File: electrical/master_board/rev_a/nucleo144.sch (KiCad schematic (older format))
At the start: 1 part, among them CN95 NUCLEO-F767ZI;2xF2x35

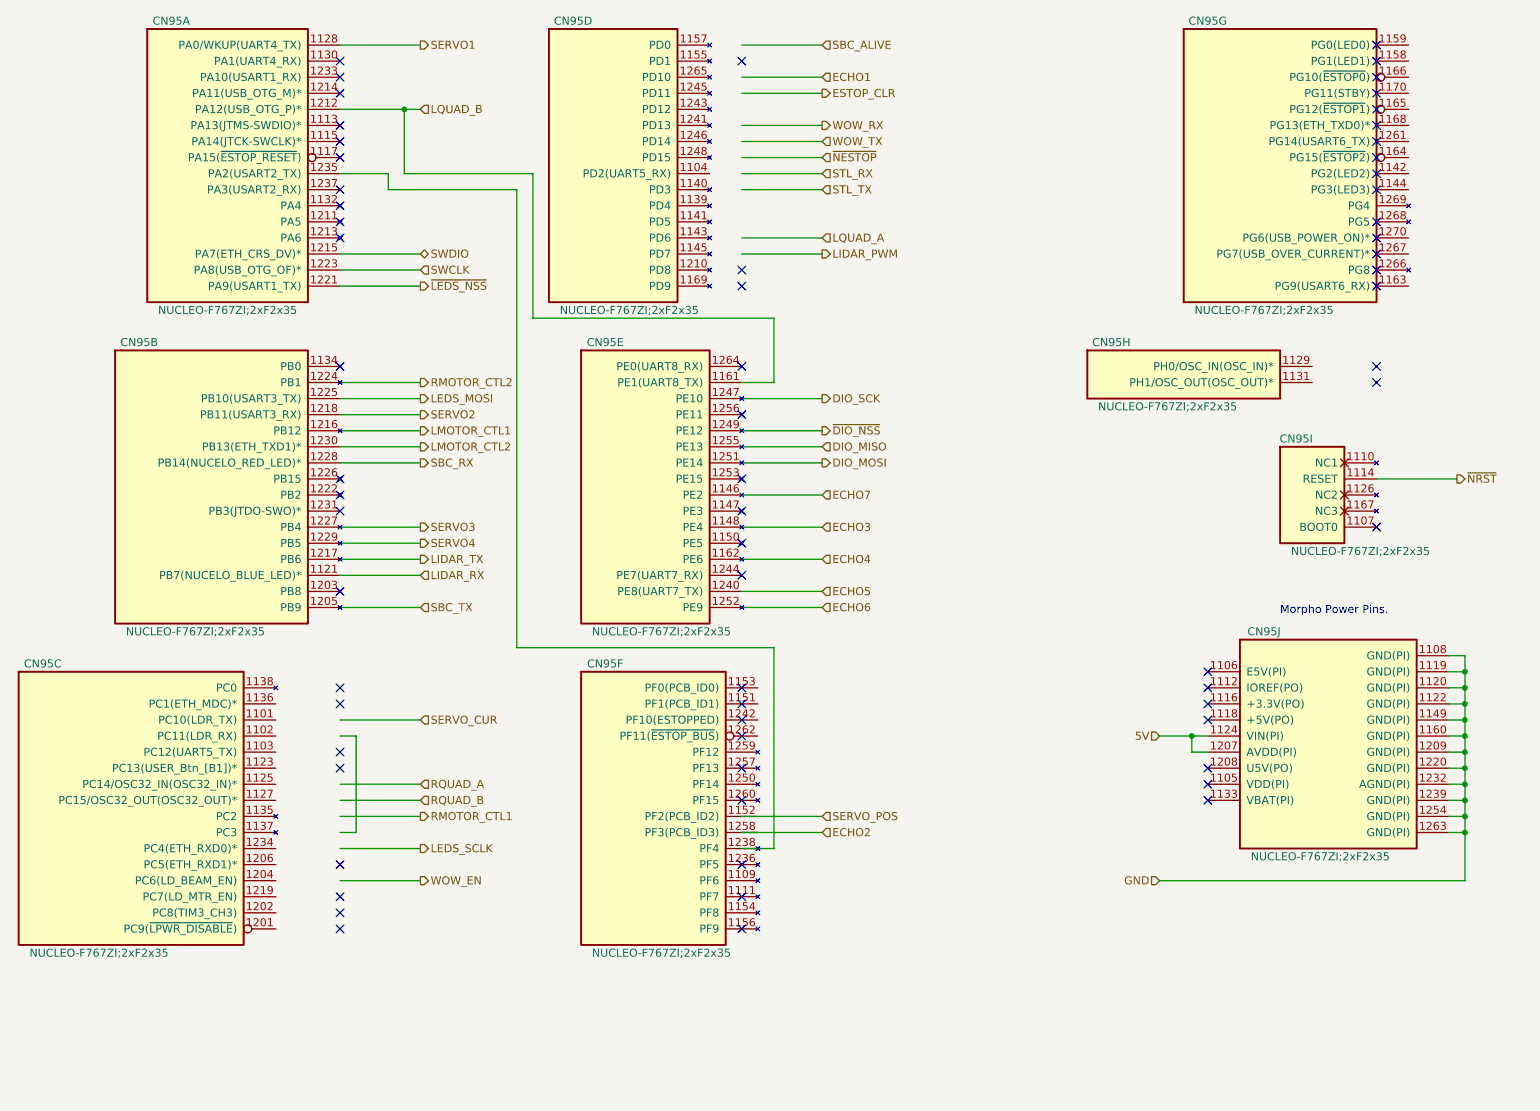
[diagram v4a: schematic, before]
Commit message: Reannoated schematic symbols.
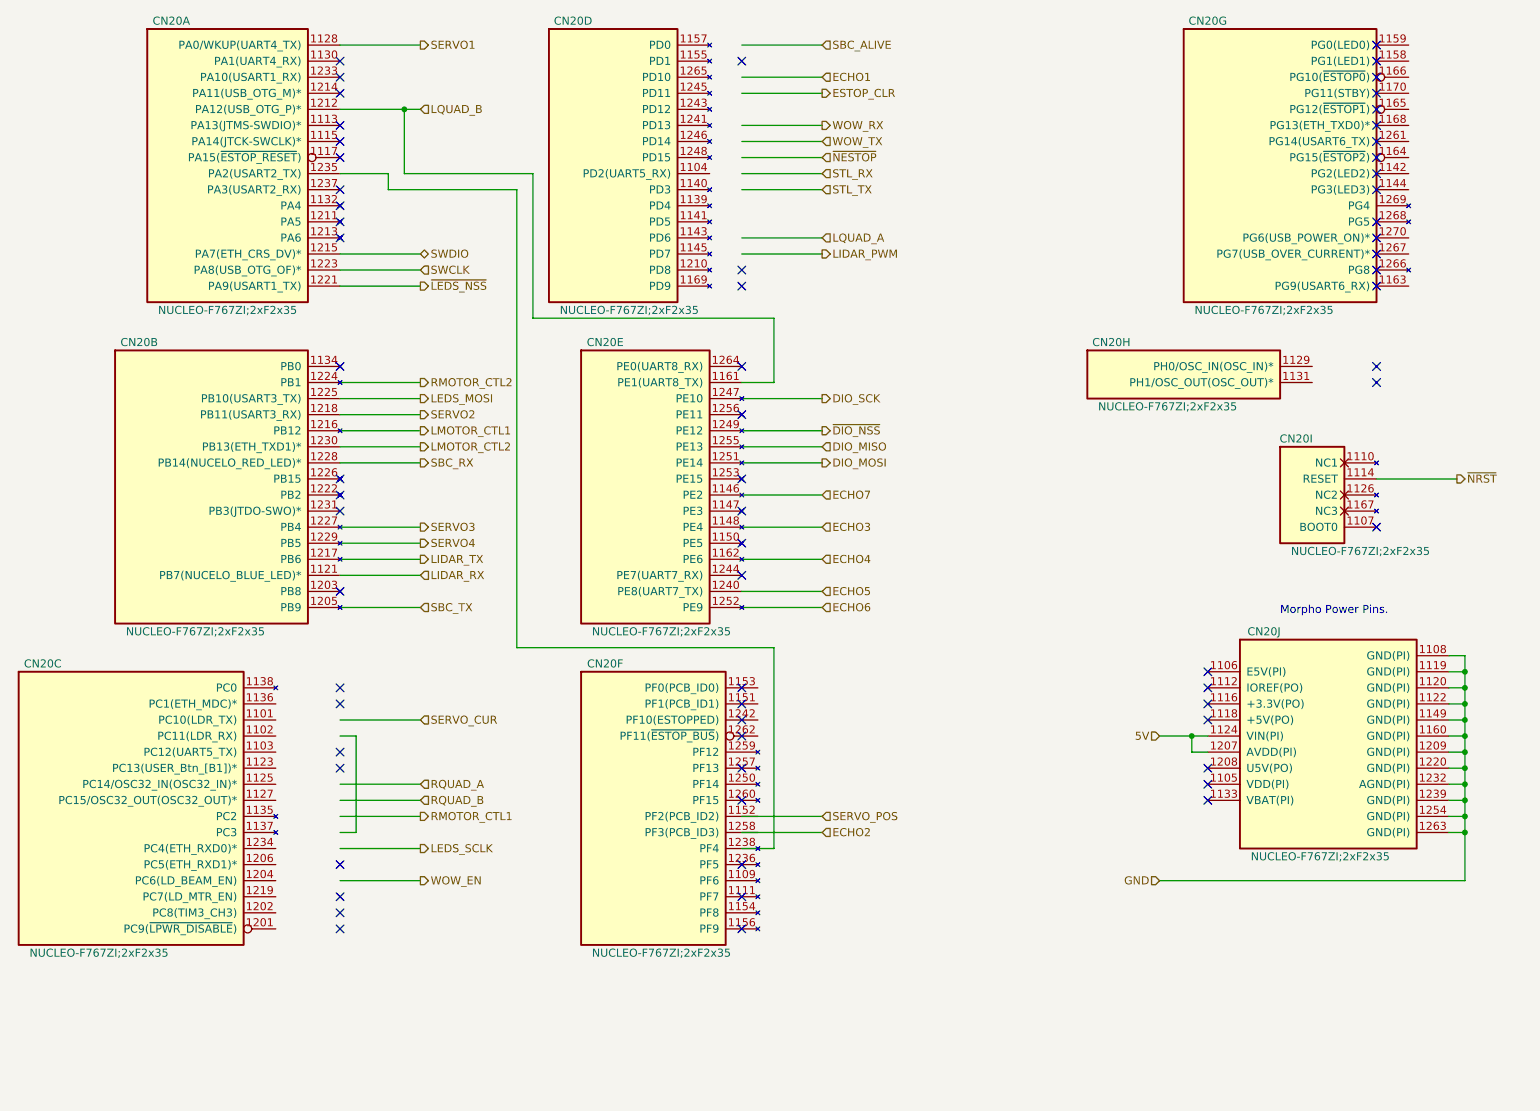
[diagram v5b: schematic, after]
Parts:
- renumbered CN95 to CN20
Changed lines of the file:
@@
 $EndDescr
 $Comp
-L HR2:NUCLEO-F767ZI;2xF2x35 CN95
+L HR2:NUCLEO-F767ZI;2xF2x35 CN20
 U 1 1 5F336099
 P 1600 800
-F 0 "CN95" H 1950 950 50  0000 C CNN
+F 0 "CN20" H 1950 950 50  0000 C CNN
 F 1 "NUCLEO-F767ZI;2xF2x35" H 2300 -850 50  0000 C CNN
 F 2 "HR2:NUCLEO_F767ZI_2xF2x35" H 1800 850 60  0001 L CNN
@@
 $EndComp
 $Comp
-L HR2:NUCLEO-F767ZI;2xF2x35 CN95
+L HR2:NUCLEO-F767ZI;2xF2x35 CN20
 U 4 1 5F34731B
 P 4100 800
-F 0 "CN95" H 4450 950 50  0000 C CNN
+F 0 "CN20" H 4450 950 50  0000 C CNN
 F 1 "NUCLEO-F767ZI;2xF2x35" H 4800 -850 50  0000 C CNN
 F 2 "HR2:NUCLEO_F767ZI_2xF2x35" H 4300 850 60  0001 L CNN
@@
 $EndComp
 $Comp
-L HR2:NUCLEO-F767ZI;2xF2x35 CN95
+L HR2:NUCLEO-F767ZI;2xF2x35 CN20
 U 6 1 5F34EC57
 P 4300 4800
-F 0 "CN95" H 4650 4950 50  0000 C CNN
+F 0 "CN20" H 4650 4950 50  0000 C CNN
 F 1 "NUCLEO-F767ZI;2xF2x35" H 5000 3150 50  0000 C CNN
 F 2 "HR2:NUCLEO_F767ZI_2xF2x35" H 4500 4850 60  0001 L CNN
@@
 $EndComp
 $Comp
-L HR2:NUCLEO-F767ZI;2xF2x35 CN95
+L HR2:NUCLEO-F767ZI;2xF2x35 CN20
 U 7 1 5F352849
 P 8050 800
-F 0 "CN95" H 8400 950 50  0000 C CNN
+F 0 "CN20" H 8400 950 50  0000 C CNN
 F 1 "NUCLEO-F767ZI;2xF2x35" H 8750 -850 50  0000 C CNN
 F 2 "HR2:NUCLEO_F767ZI_2xF2x35" H 8250 850 60  0001 L CNN
@@
 $EndComp
 $Comp
-L HR2:NUCLEO-F767ZI;2xF2x35 CN95
+L HR2:NUCLEO-F767ZI;2xF2x35 CN20
 U 9 1 5F35A1BA
 P 8650 3400
-F 0 "CN95" H 8950 3550 50  0000 C CNN
+F 0 "CN20" H 8950 3550 50  0000 C CNN
 F 1 "NUCLEO-F767ZI;2xF2x35" H 9350 2850 50  0000 C CNN
 F 2 "HR2:NUCLEO_F767ZI_2xF2x35" H 8850 3450 60  0001 L CNN
@@
 NoConn ~ 3000 1000
 $Comp
-L HR2:NUCLEO-F767ZI;2xF2x35 CN95
+L HR2:NUCLEO-F767ZI;2xF2x35 CN20
 U 10 1 5F56BA37
 P 8400 4600
-F 0 "CN95" H 8750 4750 50  0000 C CNN
+F 0 "CN20" H 8750 4750 50  0000 C CNN
 F 1 "NUCLEO-F767ZI;2xF2x35" H 9100 3350 50  0000 C CNN
 F 2 "HR2:NUCLEO_F767ZI_2xF2x35" H 8600 4650 60  0001 L CNN
@@
 SBC_ALIVE
 $Comp
-L HR2:NUCLEO-F767ZI;2xF2x35 CN95
+L HR2:NUCLEO-F767ZI;2xF2x35 CN20
 U 2 1 5F33E76C
 P 1400 2800
-F 0 "CN95" H 1750 2950 50  0000 C CNN
+F 0 "CN20" H 1750 2950 50  0000 C CNN
 F 1 "NUCLEO-F767ZI;2xF2x35" H 2100 1150 50  0000 C CNN
 F 2 "HR2:NUCLEO_F767ZI_2xF2x35" H 1600 2850 60  0001 L CNN
@@
 	5500 4300 6000 4300
 $Comp
-L HR2:NUCLEO-F767ZI;2xF2x35 CN95
+L HR2:NUCLEO-F767ZI;2xF2x35 CN20
 U 5 1 5F34B911
 P 4300 2800
-F 0 "CN95" H 4650 2950 50  0000 C CNN
+F 0 "CN20" H 4650 2950 50  0000 C CNN
 F 1 "NUCLEO-F767ZI;2xF2x35" H 5000 1150 50  0000 C CNN
 F 2 "HR2:NUCLEO_F767ZI_2xF2x35" H 4500 2850 60  0001 L CNN
@@
 NoConn ~ 9450 2800
 $Comp
-L HR2:NUCLEO-F767ZI;2xF2x35 CN95
+L HR2:NUCLEO-F767ZI;2xF2x35 CN20
 U 8 1 5F355CEA
 P 7450 2800
-F 0 "CN95" H 7800 2950 50  0000 C CNN
+F 0 "CN20" H 7800 2950 50  0000 C CNN
 F 1 "NUCLEO-F767ZI;2xF2x35" H 8150 2550 50  0000 C CNN
 F 2 "HR2:NUCLEO_F767ZI_2xF2x35" H 7650 2850 60  0001 L CNN
@@
 	3000 5400 3500 5400
 $Comp
-L HR2:NUCLEO-F767ZI;2xF2x35 CN95
+L HR2:NUCLEO-F767ZI;2xF2x35 CN20
 U 3 1 5F3444CA
 P 800 4800
-F 0 "CN95" H 1150 4950 50  0000 C CNN
+F 0 "CN20" H 1150 4950 50  0000 C CNN
 F 1 "NUCLEO-F767ZI;2xF2x35" H 1500 3150 50  0000 C CNN
 F 2 "HR2:NUCLEO_F767ZI_2xF2x35" H 1000 4850 60  0001 L CNN
